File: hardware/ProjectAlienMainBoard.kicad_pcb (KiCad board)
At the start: 2 copper layers, 69.1 x 100.6 mm, 53 parts, among them J1 Bumper, J10 Excess GPIO Pins, J3 Left Motor, J4 Right Motor, J5 Pixels, J6 Ultrasonic, J7 Micro USB, J8 I2C Multiplexer, J9 Voltage Breakout, Q1 2N3904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

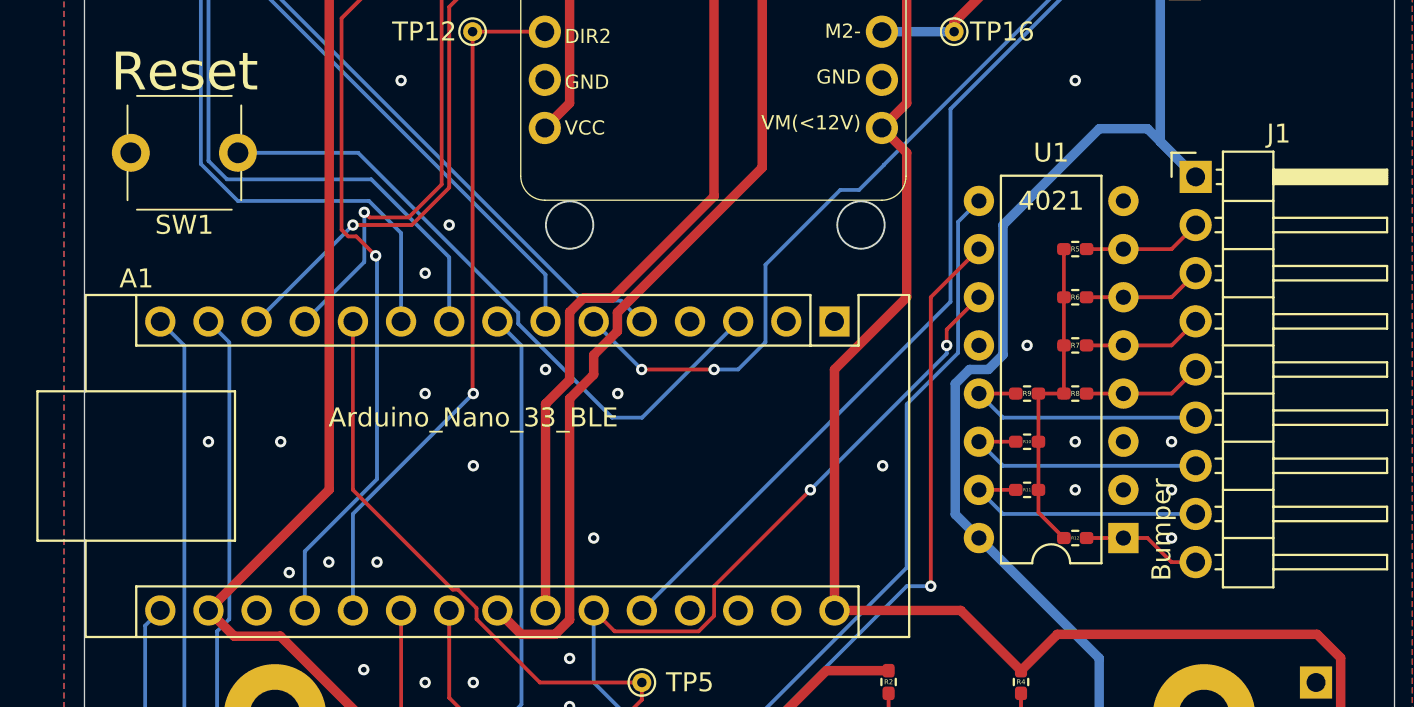
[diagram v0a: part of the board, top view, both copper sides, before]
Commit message: Tweaked silkscreen
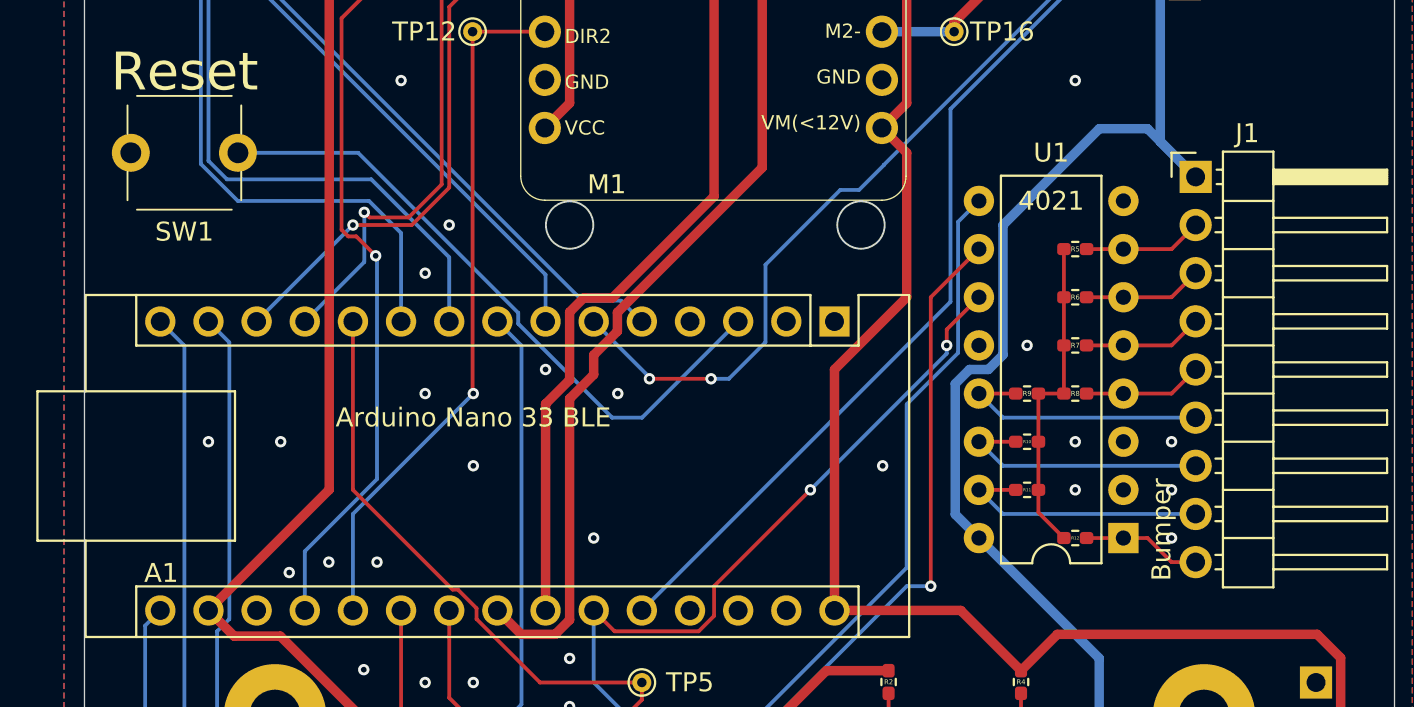
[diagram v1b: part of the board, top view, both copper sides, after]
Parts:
- A1: value Arduino_Nano_33_BLE -> Arduino Nano 33 BLE

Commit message: Generated gerber version 1
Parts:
- moved J7 0.59 mm to (153.7, 148.0)
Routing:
- net +3.3V: track 252.6 -> 251.1 mm
- net PWM2: track 28.2 -> 29.0 mm
- net SHIFT_REG_CLOCK: track 61.0 -> 60.2 mm
- net PWM1: track 29.7 -> 30.3 mm
- net M1+: track 43.4 -> 44.1 mm
- net NES_DATA: track 33.8 -> 34.4 mm
- net ENC2B: track 49.3 -> 49.9 mm
- net GND: vias 29 -> 24
